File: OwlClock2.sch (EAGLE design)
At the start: 20 parts, among them IC1 MCP1703DB, J1 AVR_SPI_PRG_6NS, J2 POWER_JACKPTH, U1 ATMEGA328P_PDIP

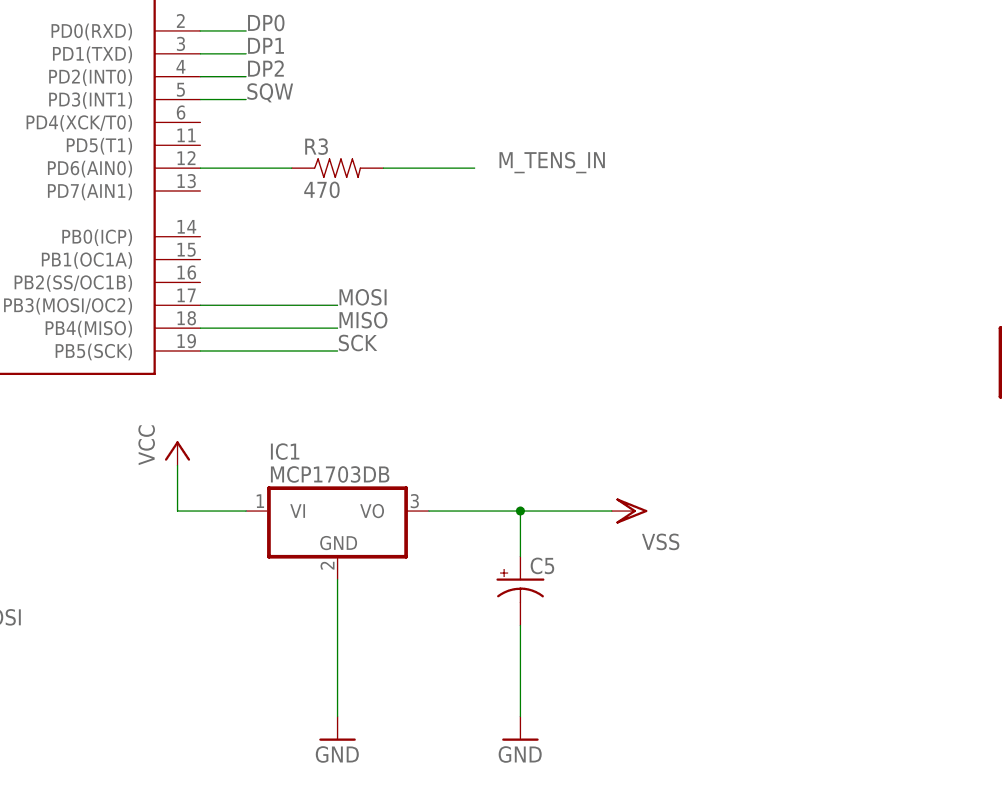
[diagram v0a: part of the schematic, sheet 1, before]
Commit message: Add vias for led grounds, clean up switches, fix up the supply caps.
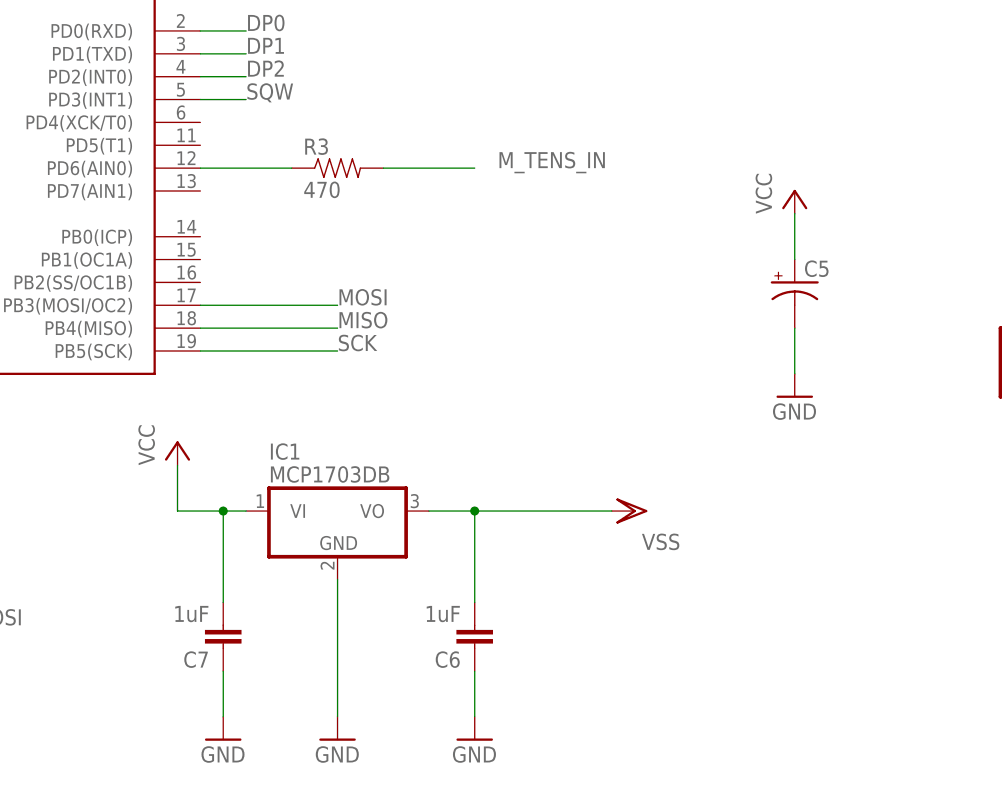
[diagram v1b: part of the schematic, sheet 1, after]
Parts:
- added C6, C7: 1uF, SparkFun-Capacitors:0.1UF-25V(+80/-20%)(0603)
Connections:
- net GND: now also C6.1, C6.2, C7.1, C7.2
- net VCC: now also C5.+, C6.1, C7.1, C7.2
- net VSS: now also C6.2; no longer C5.+
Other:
- moved on the sheet: C5
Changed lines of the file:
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@@
 <part name="VSS5" library="supply1" deviceset="VSS" device=""/>
 <part name="VSS6" library="supply1" deviceset="VSS" device=""/>
+<part name="C6" library="SparkFun-Capacitors" deviceset="0.1UF-25V(+80/-20%)(0603)" device="" value="1uF"/>
+<part name="C7" library="SparkFun-Capacitors" deviceset="0.1UF-25V(+80/-20%)(0603)" device="" value="1uF"/>
+<part name="GND6" library="supply1" deviceset="GND" device=""/>
+<part name="GND13" library="supply1" deviceset="GND" device=""/>
+<part name="P+1" library="supply1" deviceset="VCC" device=""/>
 </parts>
 <sheets>
@@
 <instance part="FRAME1" gate="G$1" x="-33.02" y="25.4"/>
 <instance part="FRAME1" gate="G$2" x="139.7" y="25.4"/>
-<instance part="GND5" gate="1" x="106.68" y="53.34"/>
+<instance part="GND5" gate="1" x="137.16" y="91.44"/>
 <instance part="C3" gate="G$1" x="17.78" y="111.76"/>
 <instance part="C4" gate="G$1" x="-17.78" y="124.46"/>
@@
 <instance part="SET" gate="G$1" x="76.2" y="203.2"/>
 <instance part="R3" gate="G$1" x="86.36" y="116.84"/>
-<instance part="C5" gate="G$1" x="106.68" y="71.12"/>
+<instance part="C5" gate="G$1" x="137.16" y="104.14"/>
 <instance part="PHOTO_INSIDE" gate="G$1" x="203.2" y="93.98"/>
 <instance part="R4" gate="G$1" x="215.9" y="78.74" rot="R90"/>
@@
 <instance part="VSS5" gate="G$1" x="175.26" y="109.22" rot="R180"/>
 <instance part="VSS6" gate="G$1" x="215.9" y="109.22" rot="R180"/>
+<instance part="C6" gate="G$1" x="101.6" y="66.04" rot="R180"/>
+<instance part="C7" gate="G$1" x="73.66" y="66.04" rot="R180"/>
+<instance part="GND6" gate="1" x="73.66" y="53.34"/>
+<instance part="GND13" gate="1" x="101.6" y="53.34"/>
+<instance part="P+1" gate="VCC" x="137.16" y="114.3"/>
 </instances>
 <busses>
@@
 <wire x1="68.58" y1="83.82" x2="68.58" y2="78.74" width="0.1524" layer="91"/>
 <pinref part="IC1" gate="G$1" pin="VI"/>
-<wire x1="68.58" y1="78.74" x2="76.2" y2="78.74" width="0.1524" layer="91"/>
+<wire x1="68.58" y1="78.74" x2="73.66" y2="78.74" width="0.1524" layer="91"/>
+<pinref part="C7" gate="G$1" pin="2"/>
+<wire x1="73.66" y1="78.74" x2="76.2" y2="78.74" width="0.1524" layer="91"/>
+<wire x1="73.66" y1="68.58" x2="73.66" y2="78.74" width="0.1524" layer="91"/>
+<junction x="73.66" y="78.74"/>
+</segment>
+<segment>
+<pinref part="C5" gate="G$1" pin="+"/>
+<pinref part="P+1" gate="VCC" pin="VCC"/>
+<wire x1="137.16" y1="106.68" x2="137.16" y2="111.76" width="0.1524" layer="91"/>
 </segment>
 </net>
@@
 <pinref part="GND5" gate="1" pin="GND"/>
 <pinref part="C5" gate="G$1" pin="-"/>
-<wire x1="106.68" y1="55.88" x2="106.68" y2="66.04" width="0.1524" layer="91"/>
+<wire x1="137.16" y1="93.98" x2="137.16" y2="99.06" width="0.1524" layer="91"/>
 </segment>
 <segment>
@@
 <pinref part="GND4" gate="1" pin="GND"/>
 <wire x1="86.36" y1="71.12" x2="86.36" y2="55.88" width="0.1524" layer="91"/>
+</segment>
+<segment>
+<pinref part="C7" gate="G$1" pin="1"/>
+<pinref part="GND6" gate="1" pin="GND"/>
+<wire x1="73.66" y1="60.96" x2="73.66" y2="55.88" width="0.1524" layer="91"/>
+</segment>
+<segment>
+<pinref part="C6" gate="G$1" pin="1"/>
+<pinref part="GND13" gate="1" pin="GND"/>
+<wire x1="101.6" y1="60.96" x2="101.6" y2="55.88" width="0.1524" layer="91"/>
 </segment>
 </net>
@@
 <net name="VSS" class="0">
 <segment>
-<pinref part="C5" gate="G$1" pin="+"/>
-<wire x1="106.68" y1="73.66" x2="106.68" y2="78.74" width="0.1524" layer="91"/>
 <pinref part="IC1" gate="G$1" pin="VO"/>
-<wire x1="96.52" y1="78.74" x2="106.68" y2="78.74" width="0.1524" layer="91"/>
 <pinref part="VSS1" gate="G$1" pin="VSS"/>
-<wire x1="116.84" y1="78.74" x2="106.68" y2="78.74" width="0.1524" layer="91"/>
-<junction x="106.68" y="78.74"/>
-</segment>
-<segment>
+<wire x1="116.84" y1="78.74" x2="101.6" y2="78.74" width="0.1524" layer="91"/>
+<pinref part="C6" gate="G$1" pin="2"/>
+<wire x1="101.6" y1="78.74" x2="96.52" y2="78.74" width="0.1524" layer="91"/>
+<wire x1="101.6" y1="68.58" x2="101.6" y2="78.74" width="0.1524" layer="91"/>
+<junction x="101.6" y="78.74"/>
+</segment>
+<segment>

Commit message: Add power plane fix board outline, finish first pass of routing.
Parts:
- C5: value (none) -> 1000uF
- JP1: value (none) -> REAL TIME CLOCK
- Q1: value (none) -> 16Mhz
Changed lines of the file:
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@@
 <part name="GND23" library="supply1" deviceset="GND" device=""/>
 <part name="R1" library="SparkFun-Resistors" deviceset="0.22OHM1/4W1%(0805)" device="" value="10k"/>
-<part name="Q1" library="adafruit" deviceset="CRYSTAL" device="HC18U-V"/>
+<part name="Q1" library="adafruit" deviceset="CRYSTAL" device="HC18U-V" value="16Mhz"/>
 <part name="C1" library="SparkFun-Capacitors" deviceset="0.1UF-25V(+80/-20%)(0603)" device="" value="22pF"/>
 <part name="C2" library="SparkFun-Capacitors" deviceset="0.1UF-25V(+80/-20%)(0603)" device="" value="0.22pF"/>
@@
 <part name="C3" library="SparkFun-Capacitors" deviceset="0.1UF-25V(+80/-20%)(0603)" device="" value="0.1uF"/>
 <part name="C4" library="SparkFun-Capacitors" deviceset="0.1UF-25V(+80/-20%)(0603)" device="" value="0.1uF"/>
-<part name="JP1" library="adafruit" deviceset="PINHD-1X6" device=""/>
+<part name="JP1" library="adafruit" deviceset="PINHD-1X6" device="" value="REAL TIME CLOCK"/>
 <part name="PHOTO_TOP" library="SparkFun-Connectors" deviceset="M02" device="LOCK"/>
 <part name="R2" library="SparkFun-Resistors" deviceset="0.22OHM1/4W1%(0805)" device="" value="10k"/>
@@
 <part name="SET" library="SparkFun-Electromechanical" deviceset="SWITCH-MOMENTARY-2" device="PTH"/>
 <part name="R3" library="SparkFun-Resistors" deviceset="0.22OHM1/4W1%(0805)" device="" value="470"/>
-<part name="C5" library="SparkFun-Capacitors" deviceset="CAP_POL" device="PTH4"/>
+<part name="C5" library="SparkFun-Capacitors" deviceset="CAP_POL" device="PTH4" value="1000uF"/>
 <part name="FRAME3" library="frames" deviceset="FRAME_A_L" device=""/>
 <part name="P+8" library="supply1" deviceset="VCC" device=""/>

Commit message: Finish up labels and cleanup, pass design rules check
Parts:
- C2: value 0.22pF -> 22pF
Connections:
- net 32K: now also U1.PB1(OC1A)
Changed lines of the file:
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@@
 <part name="Q1" library="adafruit" deviceset="CRYSTAL" device="HC18U-V" value="16Mhz"/>
 <part name="C1" library="SparkFun-Capacitors" deviceset="0.1UF-25V(+80/-20%)(0603)" device="" value="22pF"/>
-<part name="C2" library="SparkFun-Capacitors" deviceset="0.1UF-25V(+80/-20%)(0603)" device="" value="0.22pF"/>
+<part name="C2" library="SparkFun-Capacitors" deviceset="0.1UF-25V(+80/-20%)(0603)" device="" value="22pF"/>
 <part name="GND1" library="supply1" deviceset="GND" device=""/>
 <part name="GND2" library="supply1" deviceset="GND" device=""/>
@@
 <label x="203.2" y="223.52" size="1.778" layer="95"/>
 </segment>
-</net>
+<segment>
+<pinref part="U1" gate="G$1" pin="PB1(OC1A)"/>
+<wire x1="71.12" y1="106.68" x2="86.36" y2="106.68" width="0.1524" layer="91"/>
+<label x="86.36" y="106.68" size="1.778" layer="95"/>
+</segment>
+</net>

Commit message: Fix problem where real time clock was connected to the wrong supply
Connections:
- net VCC: no longer JP1.5
- net VSS: now also JP1.5
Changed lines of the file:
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@@
-</segment>
-<segment>
-<pinref part="JP1" gate="A" pin="5"/>
-<wire x1="215.9" y1="213.36" x2="203.2" y2="213.36" width="0.1524" layer="91"/>
-<label x="203.2" y="213.36" size="1.778" layer="95"/>
 </segment>
 <segment>
@@
 <pinref part="VSS6" gate="G$1" pin="VSS"/>
 </segment>
-</net>
+<segment>
+<pinref part="JP1" gate="A" pin="5"/>
+<wire x1="215.9" y1="213.36" x2="203.2" y2="213.36" width="0.1524" layer="91"/>
+<label x="203.2" y="213.36" size="1.778" layer="95"/>
+</segment>
+</net>

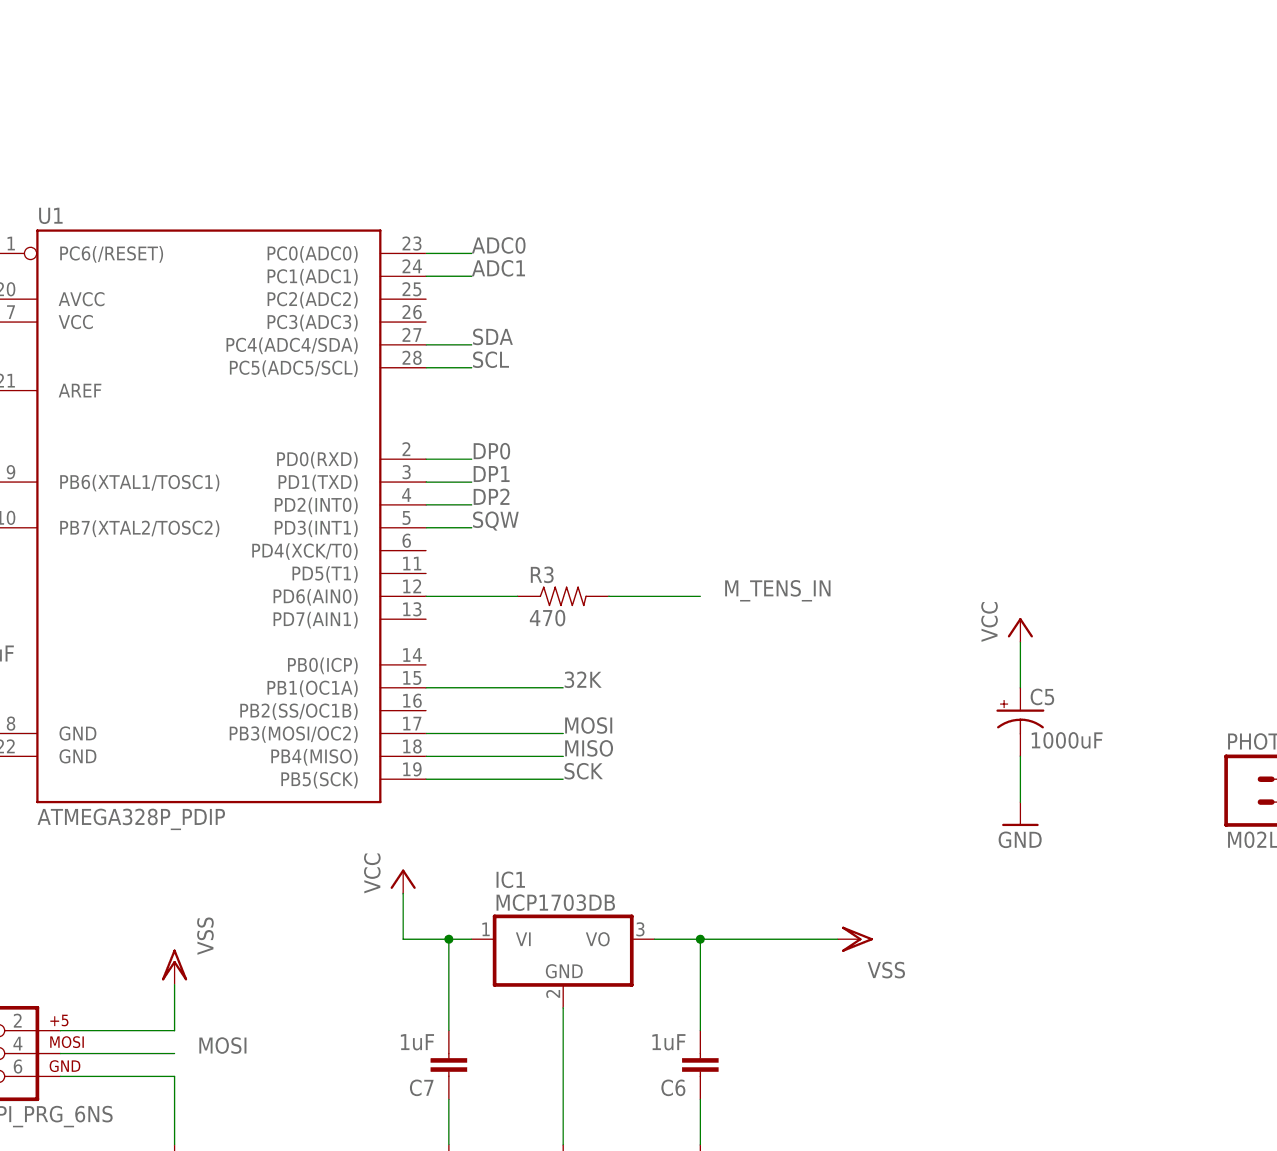
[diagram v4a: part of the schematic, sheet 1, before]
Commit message: Finally add the owlLogo to the boards and add a regulator bypass block.
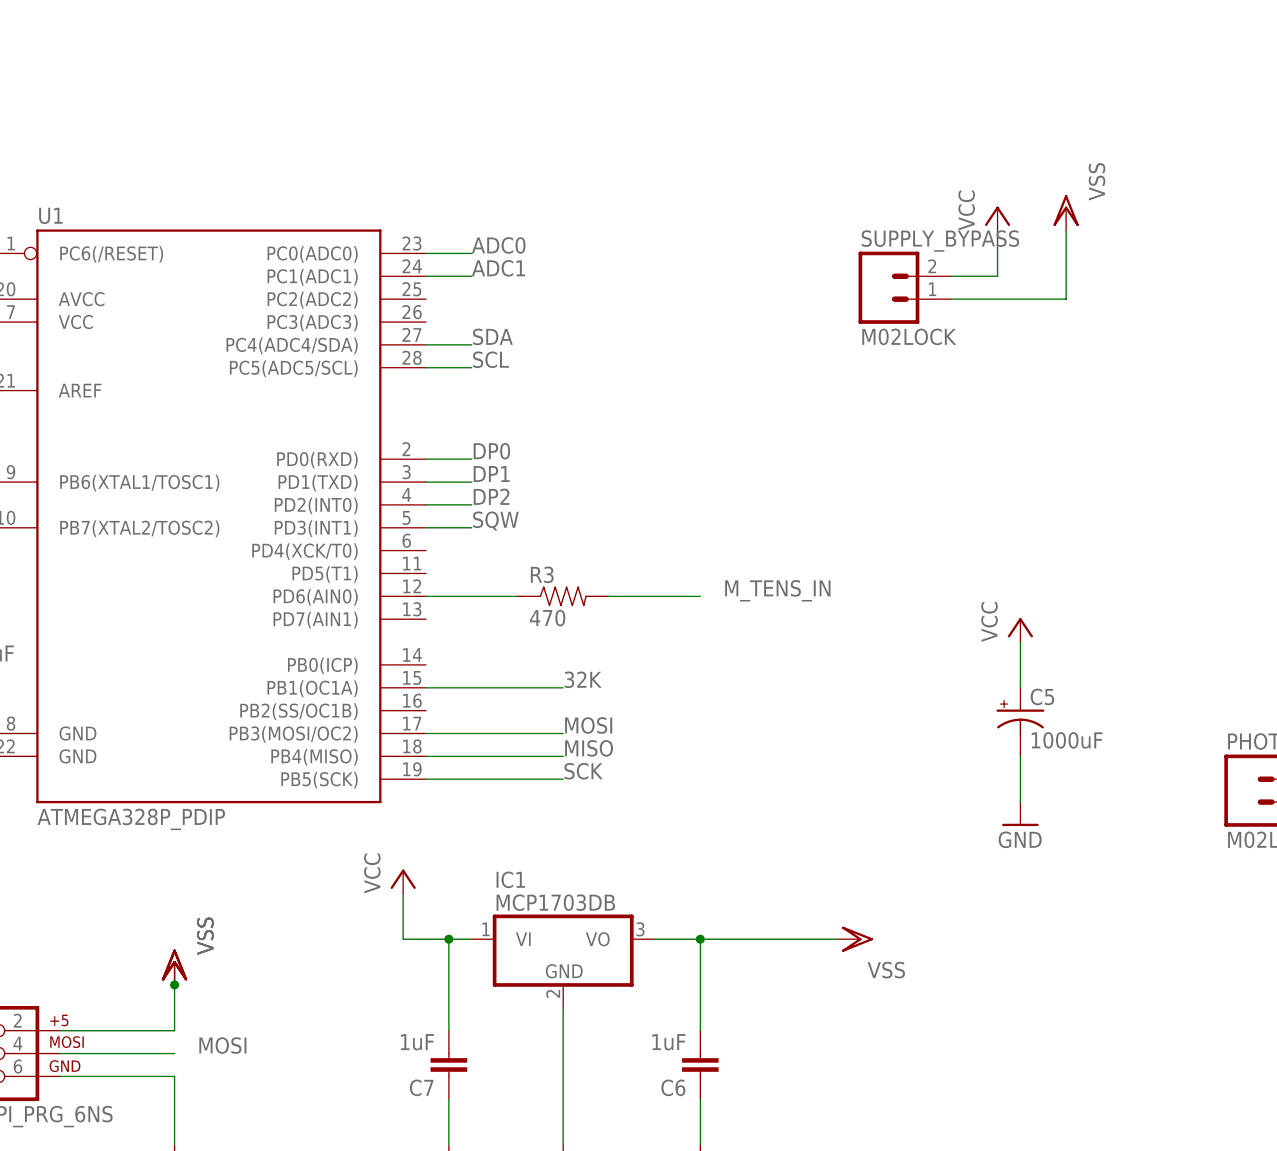
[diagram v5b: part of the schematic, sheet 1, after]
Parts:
- added SUPPLY_BYPASS: M02LOCK, SparkFun-Connectors:M02LOCK
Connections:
- net VCC: now also SUPPLY_BYPASS.2
- net VSS: now also SUPPLY_BYPASS.1
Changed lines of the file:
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@@
 <part name="GND13" library="supply1" deviceset="GND" device=""/>
 <part name="P+1" library="supply1" deviceset="VCC" device=""/>
+<part name="SUPPLY_BYPASS" library="SparkFun-Connectors" deviceset="M02" device="LOCK"/>
+<part name="P+2" library="supply1" deviceset="VCC" device=""/>
+<part name="VSS7" library="supply1" deviceset="VSS" device=""/>
+<part name="VSS8" library="supply1" deviceset="VSS" device=""/>
 </parts>
 <sheets>
@@
 <instance part="GND13" gate="1" x="101.6" y="53.34"/>
 <instance part="P+1" gate="VCC" x="137.16" y="114.3"/>
+<instance part="SUPPLY_BYPASS" gate="G$1" x="121.92" y="149.86"/>
+<instance part="P+2" gate="VCC" x="134.62" y="160.02"/>
+<instance part="VSS7" gate="G$1" x="43.18" y="76.2" rot="R180"/>
+<instance part="VSS8" gate="G$1" x="142.24" y="160.02" rot="R180"/>
 </instances>
 <busses>
@@
 <pinref part="P+1" gate="VCC" pin="VCC"/>
 <wire x1="137.16" y1="106.68" x2="137.16" y2="111.76" width="0.1524" layer="91"/>
+</segment>
+<segment>
+<pinref part="SUPPLY_BYPASS" gate="G$1" pin="2"/>
+<wire x1="129.54" y1="152.4" x2="134.62" y2="152.4" width="0.1524" layer="91"/>
+<pinref part="P+2" gate="VCC" pin="VCC"/>
+<wire x1="134.62" y1="157.48" x2="134.62" y2="152.4" width="0.1524" layer="91"/>
 </segment>
 </net>
@@
 <pinref part="VSS4" gate="G$1" pin="VSS"/>
 <wire x1="43.18" y1="68.58" x2="43.18" y2="73.66" width="0.1524" layer="91"/>
+<pinref part="VSS7" gate="G$1" pin="VSS"/>
+<junction x="43.18" y="73.66"/>
 </segment>
 <segment>
@@
 <label x="203.2" y="213.36" size="1.778" layer="95"/>
 </segment>
-</net>
+<segment>
+<pinref part="SUPPLY_BYPASS" gate="G$1" pin="1"/>
+<wire x1="129.54" y1="149.86" x2="142.24" y2="149.86" width="0.1524" layer="91"/>
+<pinref part="VSS8" gate="G$1" pin="VSS"/>
+<wire x1="142.24" y1="157.48" x2="142.24" y2="149.86" width="0.1524" layer="91"/>
+</segment>
+</net>
